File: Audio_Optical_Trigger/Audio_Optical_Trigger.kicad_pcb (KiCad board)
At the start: 2 copper layers, 58.6 x 62.4 mm, 127 parts, among them J1001 Trigger Output, J201 +12VIN, J301 TX1, J302 RX1, J401 TX2, J402 RX2, J501 TX3, J502 RX3, J901 Group Select, Q201 IRF7404, U201 74LVC1G14, U202 TPS62130, U301 74LVC1G17, U401 74LVC1G17, U501 74LVC1G17, U601 74LVC1G38, U602 74LVC1G38, U603 74LVC1G38, U701 74LVC1G38, U702 74LVC1G38, U703 74LVC1G38, U801 74LVC1G38, U802 74LVC1G38, U803 74LVC1G38, U901 74LVC1G14, U902 74LVC1G14, U903 74LVC1G14

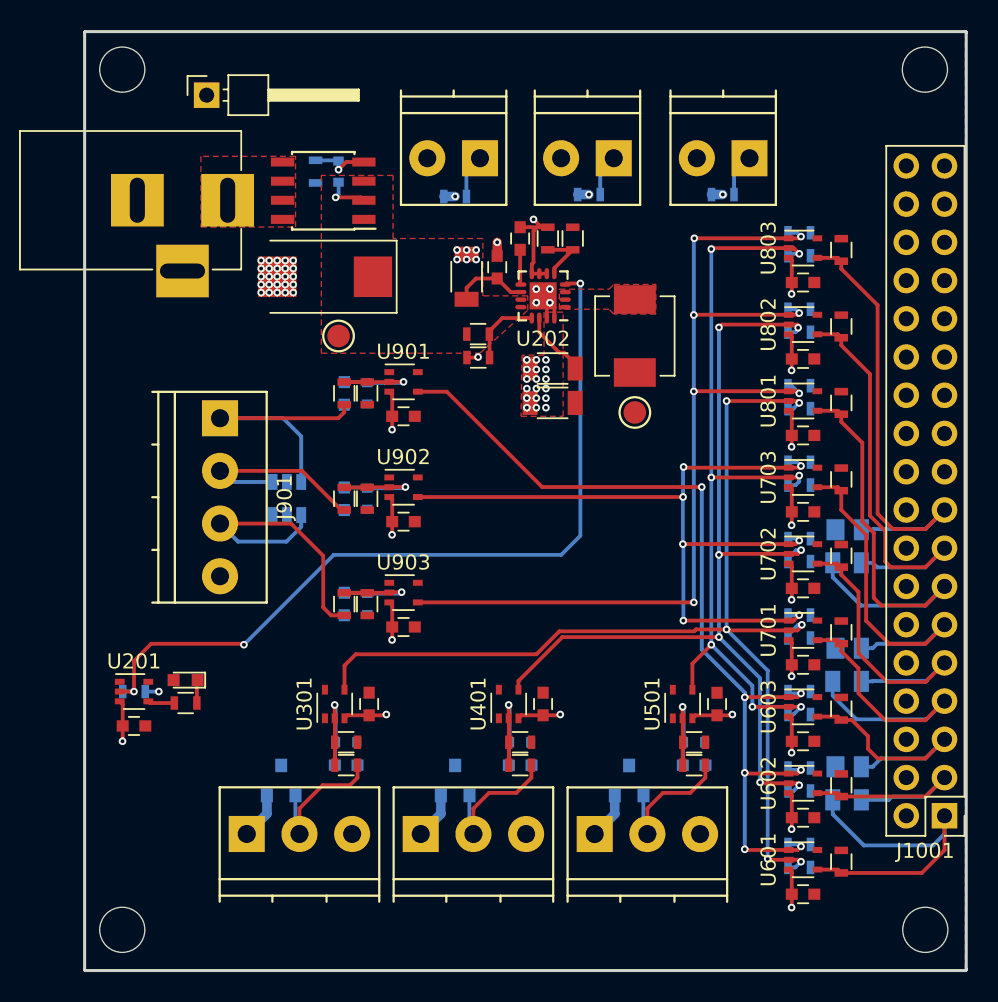
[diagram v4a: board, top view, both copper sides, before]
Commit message: Adjusted routing, design rules
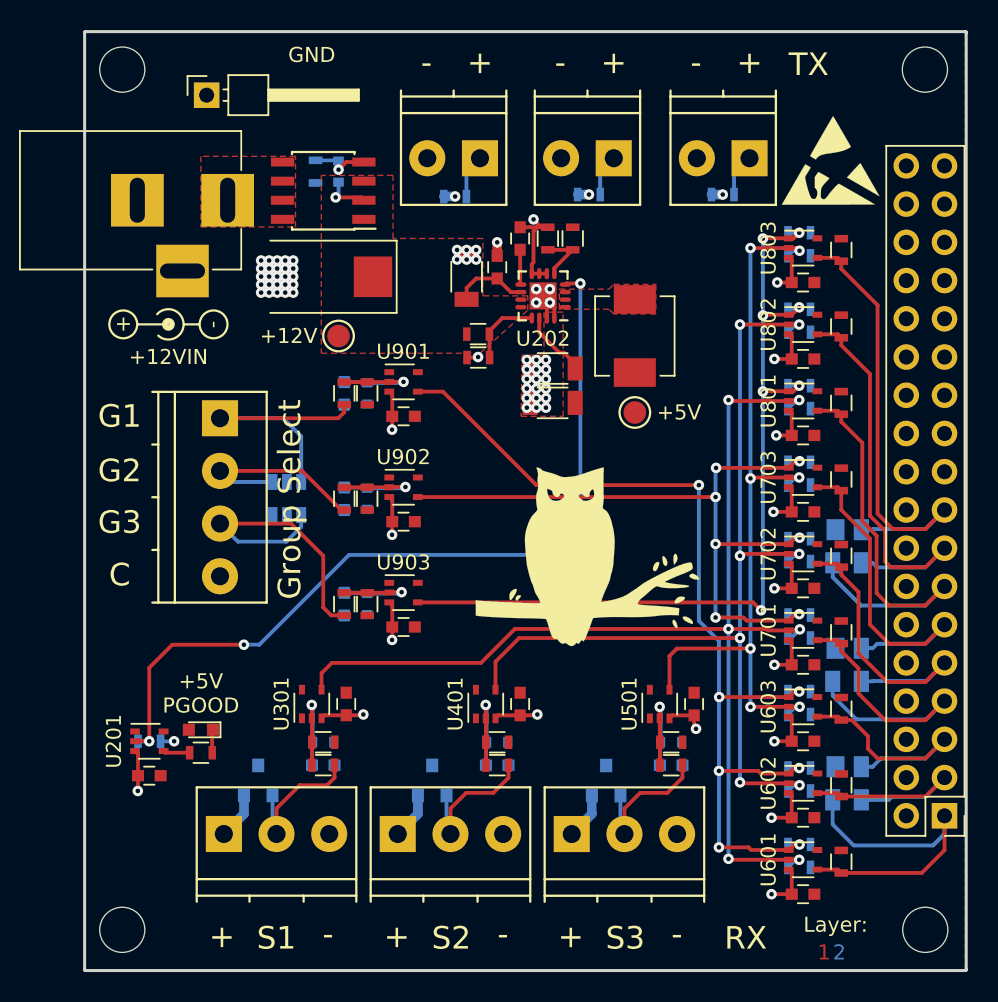
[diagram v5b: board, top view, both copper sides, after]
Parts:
- added G***: Owl_1_Logo, Custom Footprints Library:Owl_1_Logo, F.Cu at (143.4, 102.8)
- added REF**: Symbol_Barrel_Polarity, Symbols:Symbol_Barrel_Polarity, F.Cu at (115.2, 87.4)
- added REF***: ESD-Logo_6.6x6mm_SilkScreen, Symbols:ESD-Logo_6.6x6mm_SilkScreen, F.Cu at (159.2, 76.5)
- moved D202 3.45 mm to (117.3, 114.3)
- moved R202 3.45 mm to (117.3, 115.8)
- moved C201 3.45 mm to (113.9, 117.3)
- moved R203 3.45 mm to (113.9, 115.1)
- moved U201 3.45 mm to (113.9, 115.1)
- moved C301 1.52 mm to (125.5, 116.6)
- moved C302 1.52 mm to (127.0, 112.6)
- moved C401 1.52 mm to (137.0, 116.7)
- moved C402 1.52 mm to (138.6, 112.6)
- moved C501 1.52 mm to (148.6, 116.7)
- moved C502 1.52 mm to (150.1, 112.6)
- moved D301 1.52 mm to (121.2, 117.7)
- moved D302 1.52 mm to (125.5, 115.1)
- moved D401 1.52 mm to (132.7, 117.7)
- moved D402 1.52 mm to (137.0, 115.1)
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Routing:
- net Output_Group_Select_3: track 66.6 -> 57.9 mm
- net Output_Group_Select_2: track 53.9 -> 49.4 mm
- net Output_Group_Select_1: track 61.1 -> 64.7 mm
- net GND: track 52.8 -> 56.1 mm
- net Input_Channel_3: track 53.4 -> 51.0 mm
- net POS5_PGOOD: track 54.7 -> 56.7 mm
- net Input_Channel_1: track 75.3 -> 77.1 mm
- net Input_Channel_2: track 63.4 -> 64.0 mm
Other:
- net class Default: via_dia 0.508 -> 0.7; via_drill 0.254 -> 0.3
- net class Power: via_dia 0.508 -> 0.7; via_drill 0.254 -> 0.3
- net class Signal: via_dia 0.508 -> 0.7; via_drill 0.254 -> 0.3
- rule via_min_drill: 0.254 -> 0.3
- rule via_min_size: 0.508 -> 0.6
- board text added: "+"
- board text added: "+12V"
- board text added: "+12VIN"
- board text added: "+5V"
- board text added: "+5V PGOOD"
- board text added: "-"
- board text added: "1"
- board text added: "2"
- board text added: "C"
- board text added: "G1"
- board text added: "G2"
- board text added: "G3"
- board text added: "GND"
- board text added: "Group Select"
- board text added: "January 2019"
- board text added: "Layer:"
- board text added: "RX"
- board text added: "S1"
- board text added: "S2"
- board text added: "S3"
- board text added: "Sparkfun MP3 Trigger Optical Interface"
- board text added: "TX"
